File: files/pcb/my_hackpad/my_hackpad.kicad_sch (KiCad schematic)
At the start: 32 parts, among them SW1 CherryMX, SW10 CherryMX, SW11 CherryMX, SW12 CherryMX, SW13 CherryMX, SW14 CherryMX, SW15 RotaryEncoder_Switch, SW16 CherryMX, SW2 CherryMX, SW3 CherryMX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

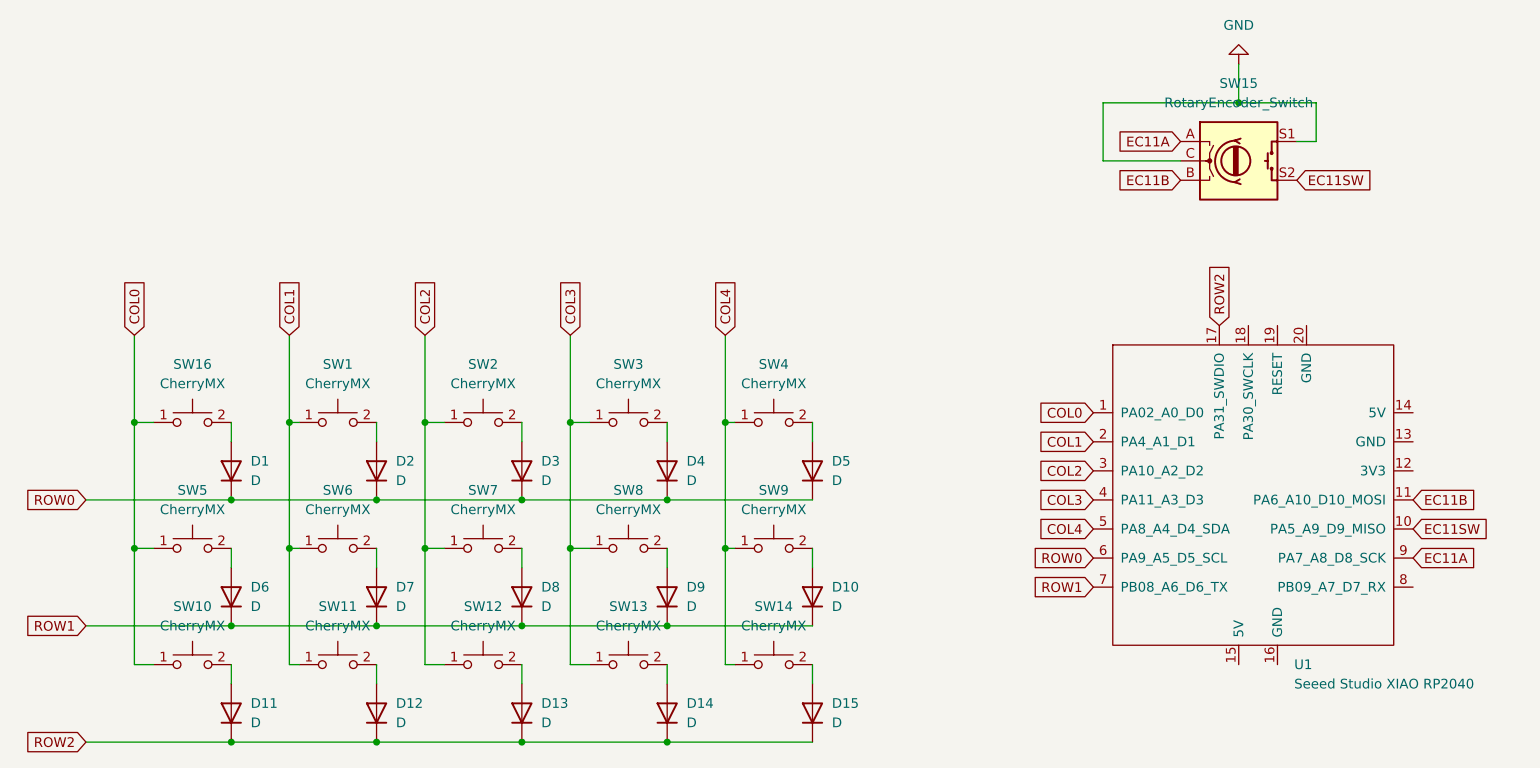
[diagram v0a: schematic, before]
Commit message: Key layout finished, wire routing started
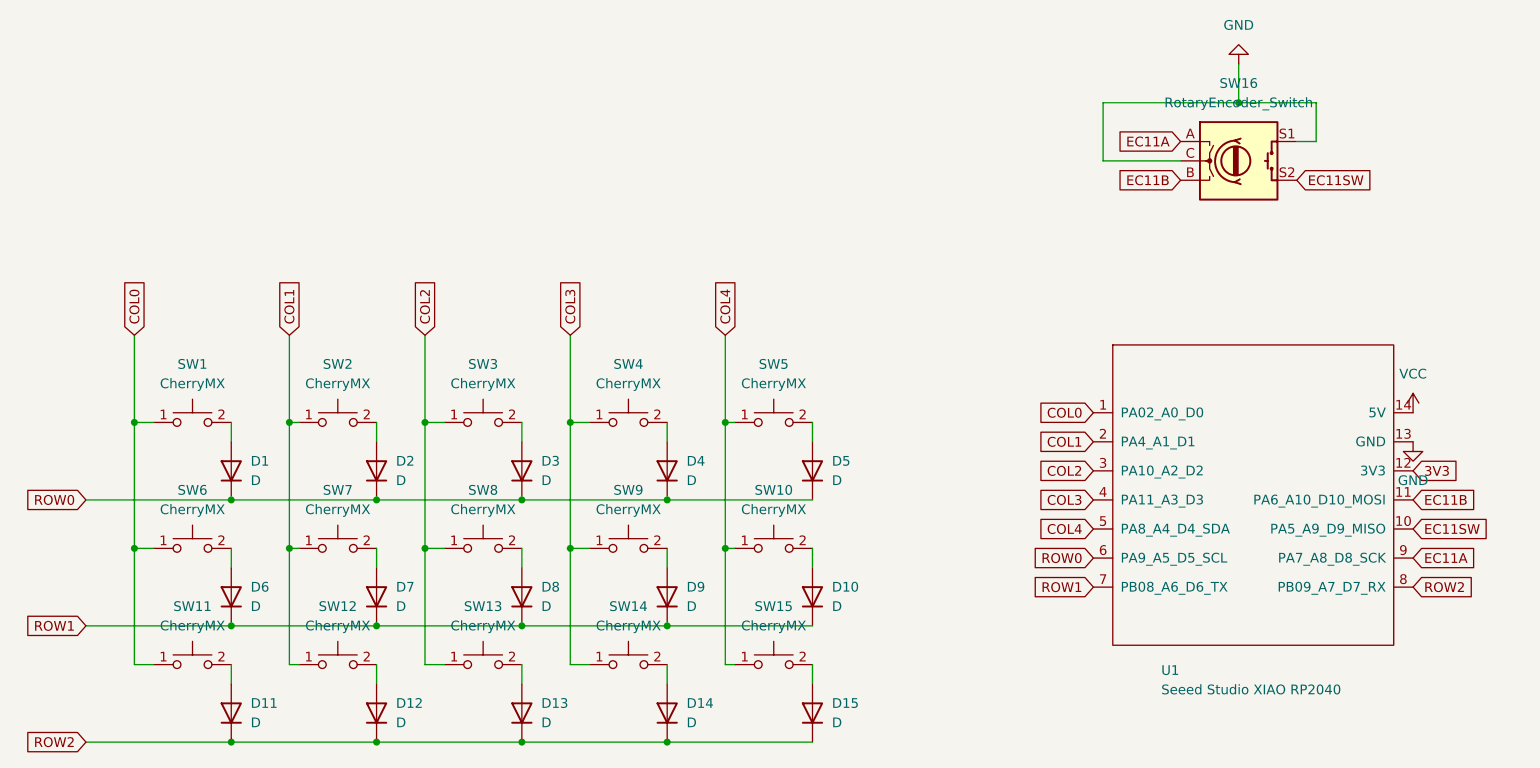
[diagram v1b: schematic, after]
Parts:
- D1, D10, D11, D12, D13, D14, D15, D2, D3, D4, D5, D6, D7, D8, D9: footprint Diode_THT:D_5KP_P10.16mm_Horizontal -> Diode_SMD:D_0805_2012Metric_Pad1.15x1.40mm_HandSolder
- SW1: renamed from SW16; footprint Switch_Keyboard_Cherry_MX:SW_Cherry_MX_PCB_4.00u -> Switch_Keyboard_Cherry_MX:SW_Cherry_MX_PCB_1.00u
- SW10: renamed from SW9; footprint Switch_Keyboard_Cherry_MX:SW_Cherry_MX_PCB_4.00u -> Switch_Keyboard_Cherry_MX:SW_Cherry_MX_PCB_1.00u
- SW11: renamed from SW10; footprint Switch_Keyboard_Cherry_MX:SW_Cherry_MX_PCB_4.00u -> Switch_Keyboard_Cherry_MX:SW_Cherry_MX_PCB_1.00u
- SW12: renamed from SW11; footprint Switch_Keyboard_Cherry_MX:SW_Cherry_MX_PCB_4.00u -> Switch_Keyboard_Cherry_MX:SW_Cherry_MX_PCB_1.00u
- SW13: renamed from SW12; footprint Switch_Keyboard_Cherry_MX:SW_Cherry_MX_PCB_4.00u -> Switch_Keyboard_Cherry_MX:SW_Cherry_MX_PCB_1.00u
- SW14: renamed from SW13; footprint Switch_Keyboard_Cherry_MX:SW_Cherry_MX_PCB_4.00u -> Switch_Keyboard_Cherry_MX:SW_Cherry_MX_PCB_1.00u
- SW15: renamed from SW14; footprint Switch_Keyboard_Cherry_MX:SW_Cherry_MX_PCB_4.00u -> Switch_Keyboard_Cherry_MX:SW_Cherry_MX_PCB_1.00u
- SW2: renamed from SW1; footprint Switch_Keyboard_Cherry_MX:SW_Cherry_MX_PCB_4.00u -> Switch_Keyboard_Cherry_MX:SW_Cherry_MX_PCB_1.00u
- SW3: renamed from SW2; footprint Switch_Keyboard_Cherry_MX:SW_Cherry_MX_PCB_4.00u -> Switch_Keyboard_Cherry_MX:SW_Cherry_MX_PCB_1.00u
- SW4: renamed from SW3; footprint Switch_Keyboard_Cherry_MX:SW_Cherry_MX_PCB_4.00u -> Switch_Keyboard_Cherry_MX:SW_Cherry_MX_PCB_1.00u
- SW5: renamed from SW4; footprint Switch_Keyboard_Cherry_MX:SW_Cherry_MX_PCB_1.50u -> Switch_Keyboard_Cherry_MX:SW_Cherry_MX_PCB_1.00u
- SW6: renamed from SW5; footprint Switch_Keyboard_Cherry_MX:SW_Cherry_MX_PCB_4.00u -> Switch_Keyboard_Cherry_MX:SW_Cherry_MX_PCB_1.00u
- SW7: renamed from SW6; footprint Switch_Keyboard_Cherry_MX:SW_Cherry_MX_PCB_4.00u -> Switch_Keyboard_Cherry_MX:SW_Cherry_MX_PCB_1.00u
- SW8: renamed from SW7; footprint Switch_Keyboard_Cherry_MX:SW_Cherry_MX_PCB_4.00u -> Switch_Keyboard_Cherry_MX:SW_Cherry_MX_PCB_1.00u
- SW9: renamed from SW8; footprint Switch_Keyboard_Cherry_MX:SW_Cherry_MX_PCB_4.00u -> Switch_Keyboard_Cherry_MX:SW_Cherry_MX_PCB_1.00u
- U1: footprint (none) -> Seeed Studio XIAO Series Library:XIAO-Generic-Thruhole-14P-2.54-21X17.8MM
- renumbered SW15 to SW16
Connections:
- net GND: now also U1.13 (GND)
- net ROW2: now also U1.8 (PB09_A7_D7_RX); no longer U1.17 (PA31_SWDIO)
- net 3V3: now reaches U1.12 (3V3)
- net VCC: now reaches U1.14 (5V)
